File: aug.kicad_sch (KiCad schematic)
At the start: 25 parts, among them J1 Conn_01x22_Socket, J2 Conn_01x22_Socket, J3 24V_IN, J4 LED_WHITE, J5 LED_RED, J6 Display Connector, J7 BME280 Connector, Q1 SI2356DS-T1-BE3, Q2 SI2356DS-T1-BE3, U1 TSR1-2450E

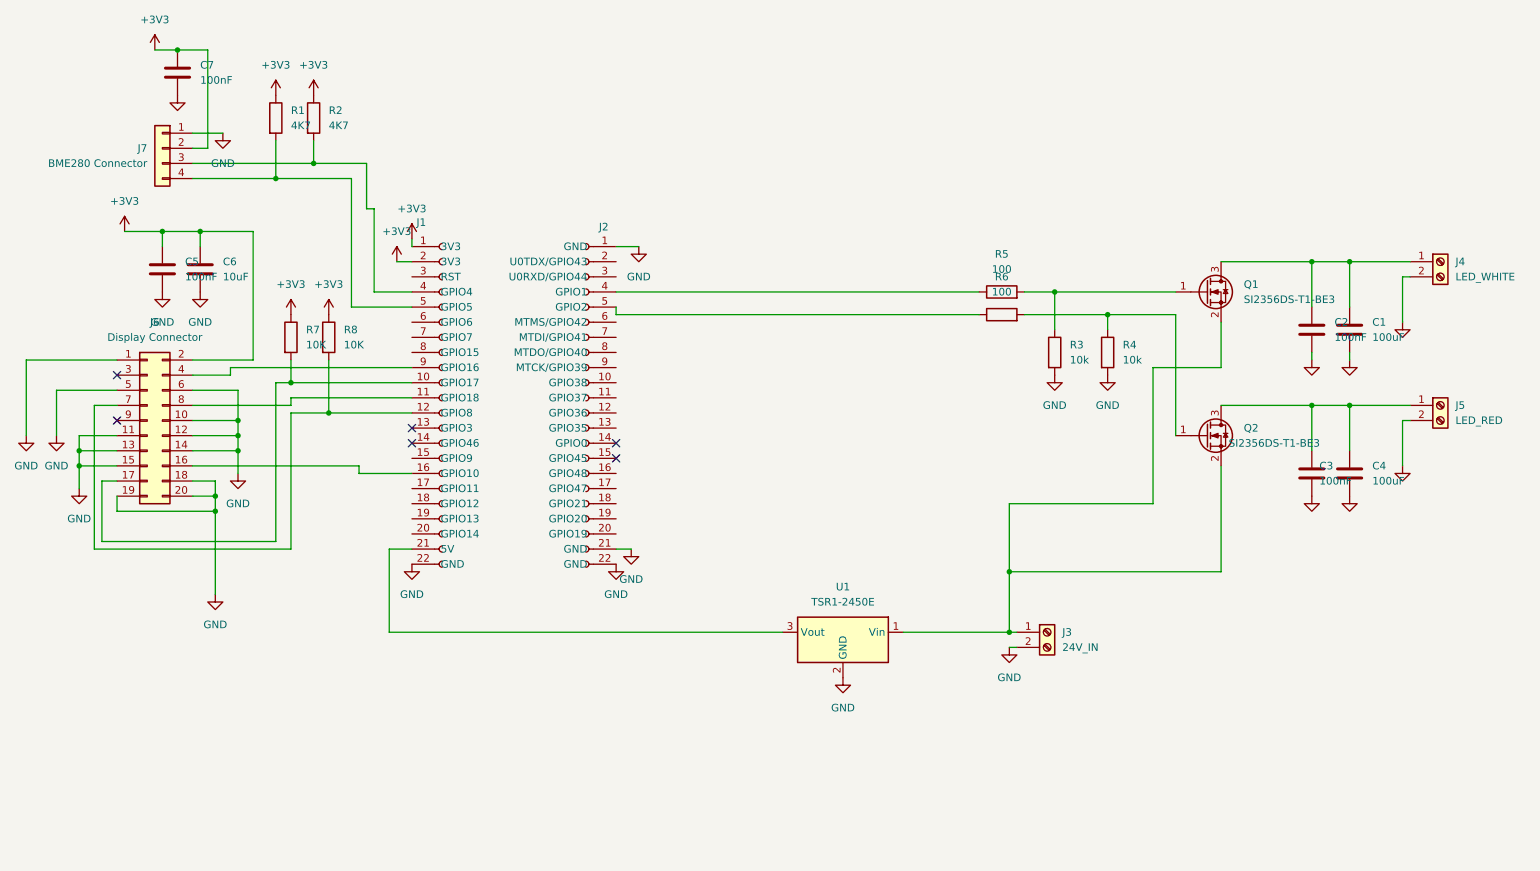
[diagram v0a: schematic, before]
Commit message: PCB version 1. Ordered.
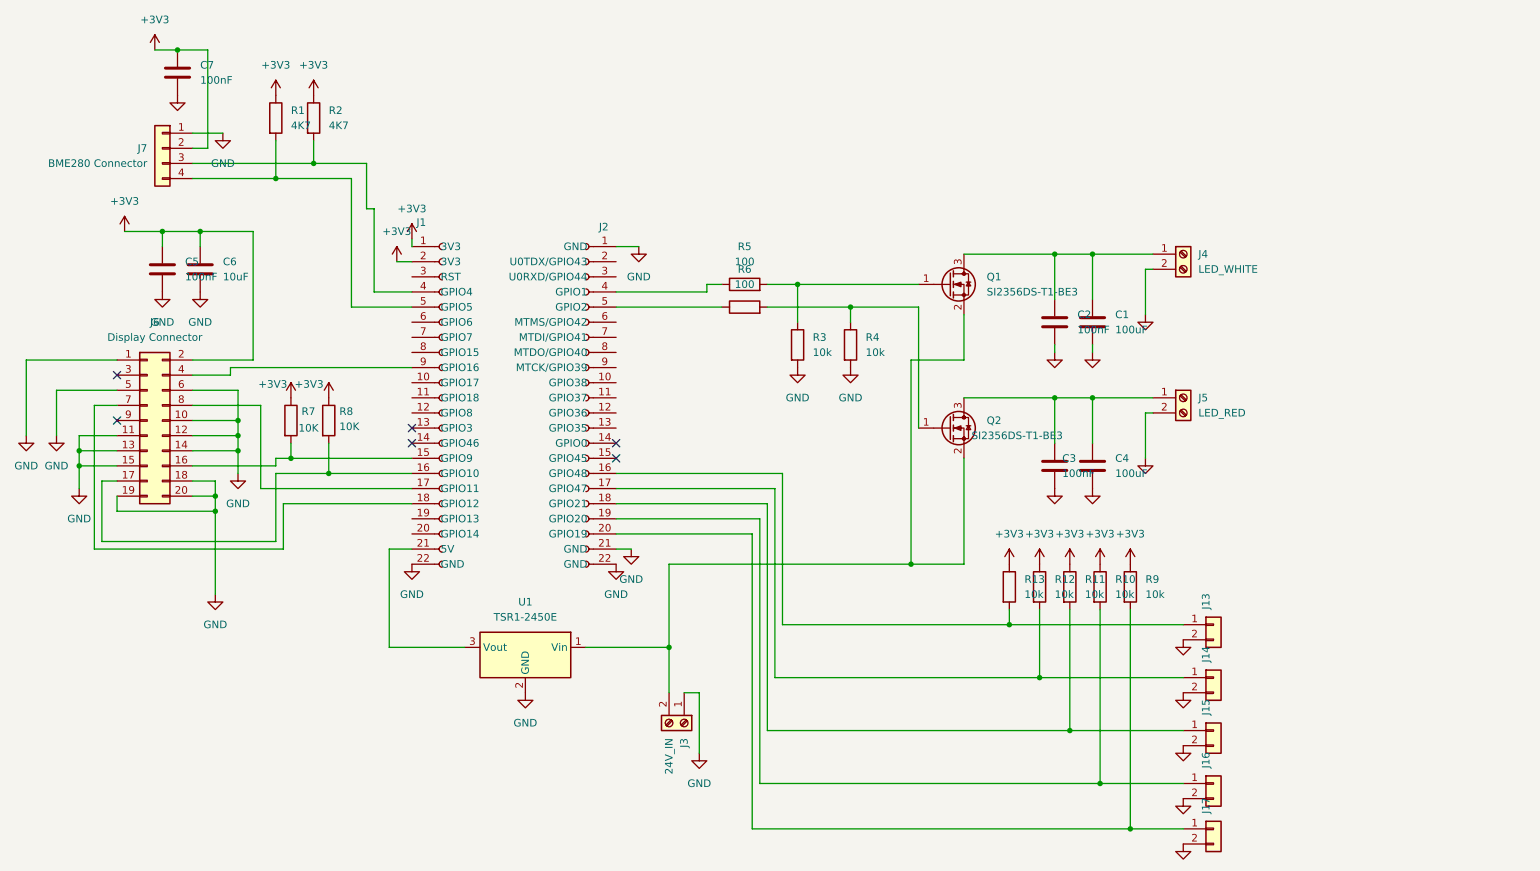
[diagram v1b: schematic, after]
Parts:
- added J13, J14, J15, J16, J17: Conn_01x02, Connector_PinHeader_2.54mm:PinHeader_1x02_P2.54mm_Vertical, symbol Connector_Generic:Conn_01x02
- added R10, R11, R12, R13, R9: 10k, Resistor_SMD:R_0805_2012Metric, symbol Device:R
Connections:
- net +3V3: now also R10.1, R11.1, R12.1, R13.1, R9.1
- net GND: now also J3.1 (Pin_1), J13.2 (Pin_2), J14.2 (Pin_2), J15.2 (Pin_2), J16.2 (Pin_2), J17.2 (Pin_2); no longer J3.2 (Pin_2)
- net at Q1.2 (S), Q2.2 (S), U1.1 (Vin): now also J3.2 (Pin_2); no longer J3.1 (Pin_1)
- net at J2.16 (GPIO48): now also J13.1 (Pin_1), R13.2
- net at J2.17 (GPIO47): now also J14.1 (Pin_1), R12.2
- net at J2.18 (GPIO21): now also J15.1 (Pin_1), R11.2
- net at J2.19 (GPIO20): now also J16.1 (Pin_1), R10.2
- net at J2.20 (GPIO19): now also J17.1 (Pin_1), R9.2
- net at J1.11 (GPIO18): no longer J6.8 (SDIN)
- net at J1.15 (GPIO9): now also J6.16 (!RES), R7.2
- net at J1.16 (GPIO10): now also J6.17 (!CS), R8.2; no longer J6.16 (!RES)
- net at J1.17 (GPIO11): now also J6.8 (SDIN)
- net at J1.18 (GPIO12): now also J6.7 (SCLK)
- now unconnected: J1.10 (GPIO17), J1.12 (GPIO8)
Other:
- moved on the sheet: C1, C2, C3, C4, J3, J4, J5, Q1, Q2, R3, R4, R5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
